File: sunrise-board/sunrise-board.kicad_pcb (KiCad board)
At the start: 2 copper layers, 25.4 x 95.2 mm, 32 parts, among them J1 Barrel Jack 12V, J2 Header, J3 FTDI Basic, J4 Header, J5 LED_STRIP_VGRB, J6 I2C, Q1 IRLZ34N, Q2 IRLZ34N, Q3 IRLZ34N, SW1 Reset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

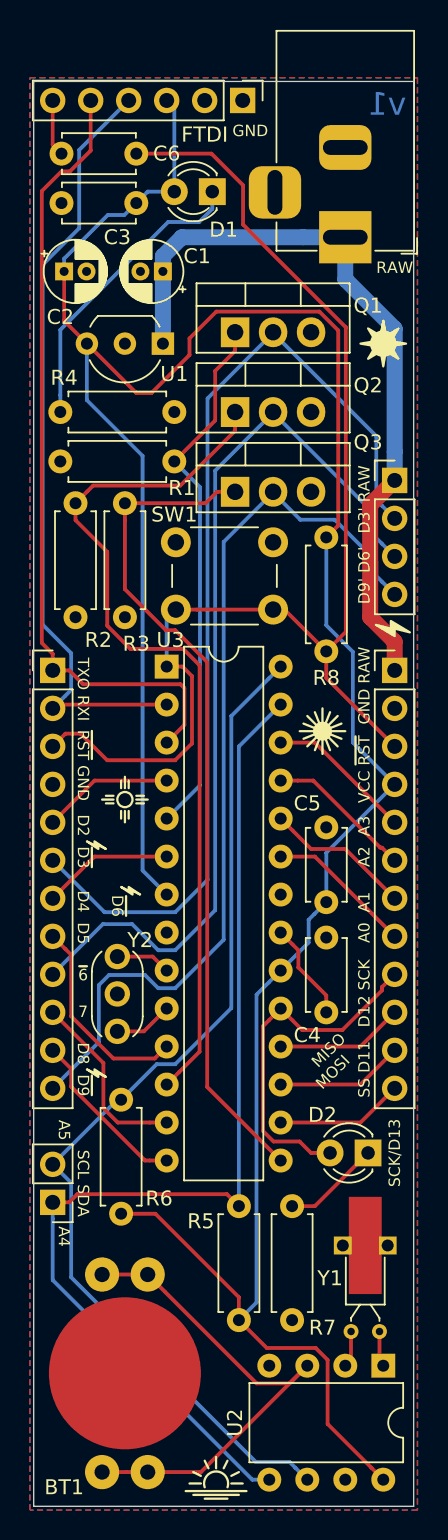
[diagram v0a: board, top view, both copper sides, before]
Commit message: fix board layout
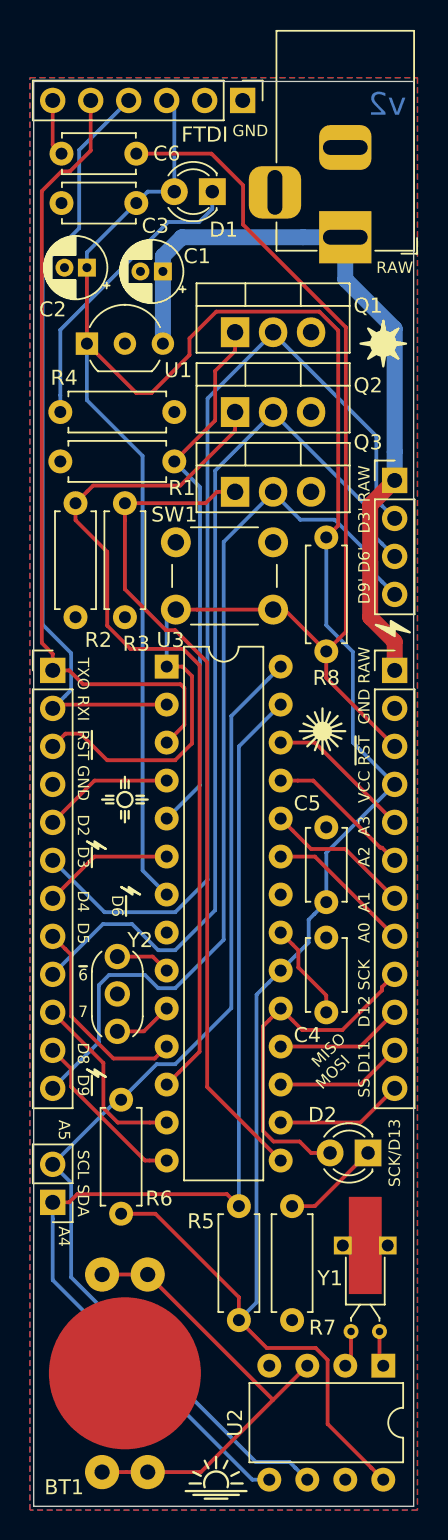
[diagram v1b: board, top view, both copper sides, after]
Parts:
- J1: value Barrel Jack 12V -> 2.1mm Jack
- J5: value LED_STRIP_VGRB -> Header
- J6: value I2C -> Header
- Q1, Q2, Q3: value IRLZ34N -> STP16NF06
- R4, R5, R6, R8: value 10K -> 10k
- U1: value L4931CZ50-AP -> L4931
- moved U1 5.08 mm to (129.3, 67.1), turned to 0 degrees
- moved C2 1.55 mm to (129.3, 62.0), turned to 180 degrees
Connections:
- U1 pad 1: RAW -> VCC
- U1 pad 3: VCC -> RAW
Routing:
- net Net-(BT1-Pad1): track 33.9 -> 31.6 mm
- net VCC: track 183.5 -> 181.6 mm
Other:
- board text added: "v2"
- board text removed: "v1"

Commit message: regen gerbers
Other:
- board text added: "~D3~ RAW"
- board text added: "~D9~ ~D6~"
- board text removed: "D3' RAW"
- board text removed: "D9' D6'"
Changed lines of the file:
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@@
       (effects (font (size 1 1) (thickness 0.15)))
     )
-    (fp_text value 32.768Hz (at -1.016 5.334 270) (layer F.Fab)
+    (fp_text value 32.768Hz (at -1.524 5.588 270) (layer F.Fab)
       (effects (font (size 1 1) (thickness 0.15)))
     )
@@
       (effects (font (size 1 1) (thickness 0.15)))
     )
-    (fp_text value STP16NF06 (at 4.064 -0.254) (layer F.Fab)
+    (fp_text value STP16NF06 (at 11.938 -3.048) (layer F.Fab)
       (effects (font (size 1 1) (thickness 0.15)))
     )
@@
     (fp_line (start 7.79 1.51) (end 7.79 -3.4) (layer F.CrtYd) (width 0.05))
     (fp_line (start 7.79 -3.4) (end -2.71 -3.4) (layer F.CrtYd) (width 0.05))
-    (fp_text user %R (at -1.016 -0.254) (layer F.Fab)
+    (fp_text user %R (at 2.54 -0.254) (layer F.Fab)
       (effects (font (size 1 1) (thickness 0.15)))
     )
@@
       (effects (font (size 1 1) (thickness 0.15)))
     )
-    (fp_text value STP16NF06 (at 4.064 -0.254) (layer F.Fab)
-      (effects (font (size 1 1) (thickness 0.15)))
-    )
-    (fp_text user %R (at -1.016 -0.254) (layer F.Fab)
+    (fp_text value STP16NF06 (at 11.938 -1.016) (layer F.Fab)
+      (effects (font (size 1 1) (thickness 0.15)))
+    )
+    (fp_text user %R (at 2.54 -0.254) (layer F.Fab)
       (effects (font (size 1 1) (thickness 0.15)))
     )
@@
       (effects (font (size 1 1) (thickness 0.15)))
     )
-    (fp_text value STP16NF06 (at 4.064 -0.254) (layer F.Fab)
+    (fp_text value STP16NF06 (at 11.938 -1.016) (layer F.Fab)
       (effects (font (size 1 1) (thickness 0.15)))
     )
@@
     (fp_line (start 7.79 1.51) (end 7.79 -3.4) (layer F.CrtYd) (width 0.05))
     (fp_line (start 7.79 -3.4) (end -2.71 -3.4) (layer F.CrtYd) (width 0.05))
-    (fp_text user %R (at -0.762 -0.254) (layer F.Fab)
+    (fp_text user %R (at 2.54 -0.254) (layer F.Fab)
       (effects (font (size 1 1) (thickness 0.15)))
     )
@@
       (effects (font (size 1 1) (thickness 0.15)))
     )
-    (fp_text value Header (at 0 2.286 90) (layer F.Fab)
+    (fp_text value Header (at 2.54 1.27 90) (layer F.Fab)
       (effects (font (size 1 1) (thickness 0.15)))
     )
@@
     (fp_line (start 1.8 4.35) (end 1.8 -1.8) (layer F.CrtYd) (width 0.05))
     (fp_line (start 1.8 -1.8) (end -1.8 -1.8) (layer F.CrtYd) (width 0.05))
-    (fp_text user %R (at 0 0 270) (layer F.Fab)
+    (fp_text user %R (at 0 1.27 270) (layer F.Fab)
       (effects (font (size 1 1) (thickness 0.15)))
     )
@@
       (effects (font (size 1 1) (thickness 0.15)))
     )
-    (fp_text value Header (at 0 9.906 90) (layer F.Fab)
+    (fp_text value Header (at 2.54 13.97 90) (layer F.Fab)
       (effects (font (size 1 1) (thickness 0.15)))
     )
@@
       (effects (font (size 1 1) (thickness 0.15)))
     )
-    (fp_text value "FTDI Basic" (at 0 2.794) (layer F.Fab)
+    (fp_text value "FTDI Basic" (at -2.54 6.35) (layer F.Fab)
       (effects (font (size 1 1) (thickness 0.15)))
     )
@@
     (fp_line (start 1.8 14.5) (end 1.8 -1.8) (layer F.CrtYd) (width 0.05))
     (fp_line (start 1.8 -1.8) (end -1.8 -1.8) (layer F.CrtYd) (width 0.05))
-    (fp_text user %R (at 0 8.636) (layer F.Fab)
+    (fp_text user %R (at 0 6.35) (layer F.Fab)
       (effects (font (size 1 1) (thickness 0.15)))
     )
@@
       (effects (font (size 1 1) (thickness 0.15)))
     )
-    (fp_text value Header (at 0 9.906 90) (layer F.Fab)
+    (fp_text value Header (at -2.54 13.97 90) (layer F.Fab)
       (effects (font (size 1 1) (thickness 0.15)))
     )
@@
       (effects (font (size 1 1) (thickness 0.15)))
     )
-    (fp_text value "2.1mm Jack" (at -7.112 -3.556 270) (layer F.Fab)
+    (fp_text value "2.1mm Jack" (at -5.08 -3.556 270) (layer F.Fab)
       (effects (font (size 1 1) (thickness 0.15)))
     )
@@
     (effects (font (size 0.762 0.762) (thickness 0.1524)))
   )
-  (gr_text "D9' D6'" (at 147.828 82.55 90) (layer F.SilkS)
+  (gr_text "~D9~  ~D6~" (at 147.828 82.55 90) (layer F.SilkS)
     (effects (font (size 0.762 0.762) (thickness 0.1524)))
   )
@@
   (gr_circle (center 138.43 120.65) (end 140.97 120.65) (layer B.SilkS) (width 10.16))
   (gr_poly (pts (xy 148.59 85.852) (xy 149.86 86.614) (xy 149.86 86.106) (xy 150.876 86.36) (xy 149.606 85.598) (xy 149.606 86.106)) (layer F.SilkS) (width 0.15))
-  (gr_text "D3' RAW" (at 147.828 77.47 90) (layer F.SilkS)
+  (gr_text " ~D3~ RAW" (at 147.828 77.47 90) (layer F.SilkS)
     (effects (font (size 0.762 0.762) (thickness 0.1524)))
   )
